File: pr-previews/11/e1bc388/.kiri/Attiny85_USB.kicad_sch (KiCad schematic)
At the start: 18 parts, among them J1 Conn_01x04, J2 Conn_01x04, T1 CST1, U1 ATtiny85-20M

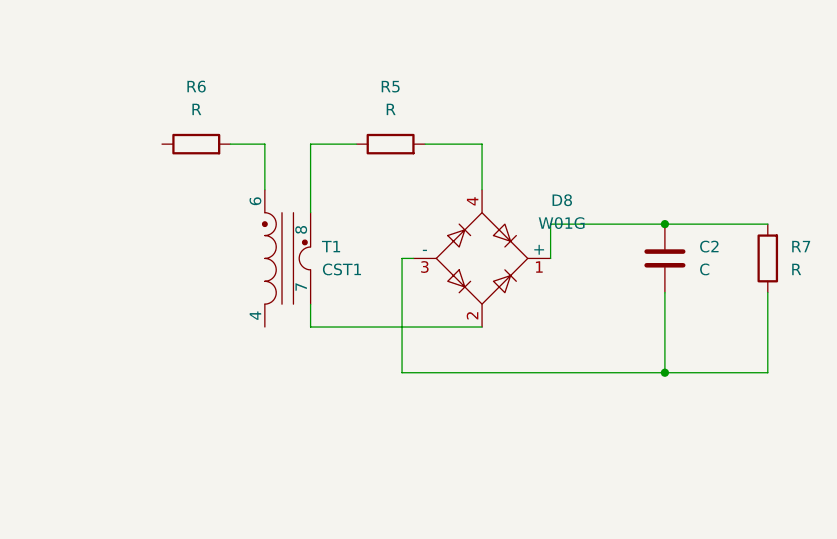
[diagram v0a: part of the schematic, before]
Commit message: Update Kiri output for PR #11
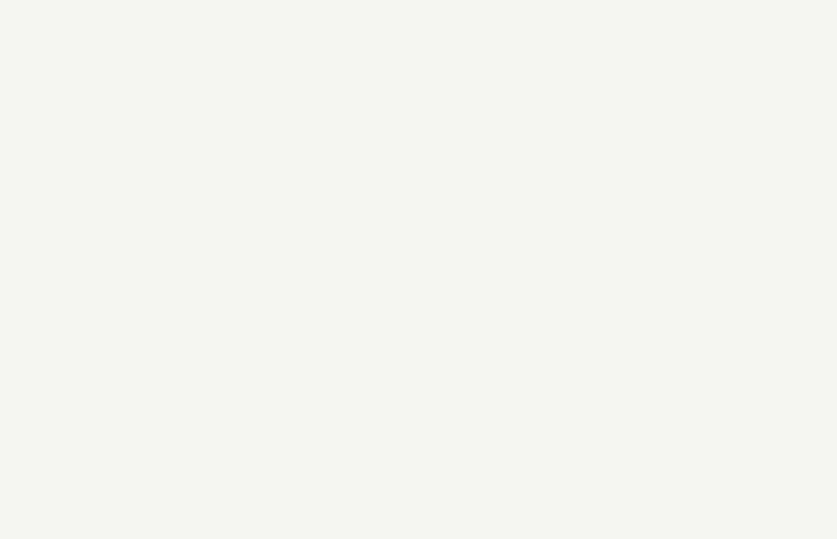
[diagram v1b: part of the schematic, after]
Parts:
- removed C2: C, Capacitor_SMD:C_0201_0603Metric, symbol Device:C
- removed D8: W01G, Diode_THT:Diode_Bridge_Round_D9.8mm, symbol Diode_Bridge:W01G
- removed R5, R6, R7: R, Resistor_SMD:R_0508_1220Metric_Pad1.12x2.15mm_HandSolder, symbol Device:R
- removed T1: CST1, Transformer_SMD:Transformer_Coilcraft_CST1, symbol Transformer:CST1
